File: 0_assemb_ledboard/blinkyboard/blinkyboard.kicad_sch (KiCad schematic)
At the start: 61 parts, among them J1 Conn_01x05, U1 LM2902, U2 LM2902, U3 LM2902, U4 LM2902

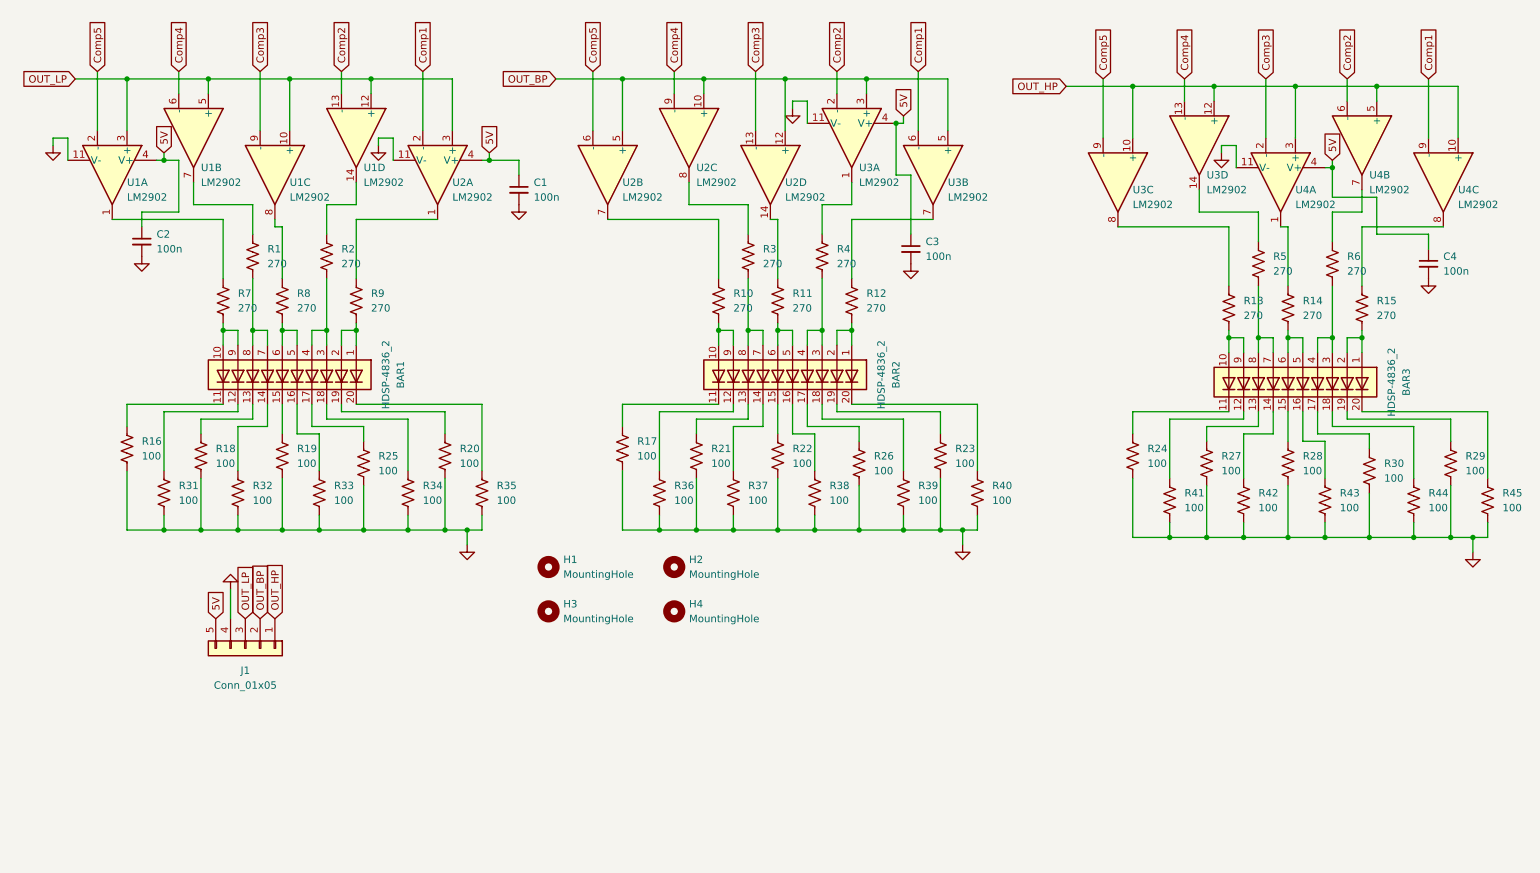
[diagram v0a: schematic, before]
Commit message: Fixed LED Board and added GND to SPI on Main Board
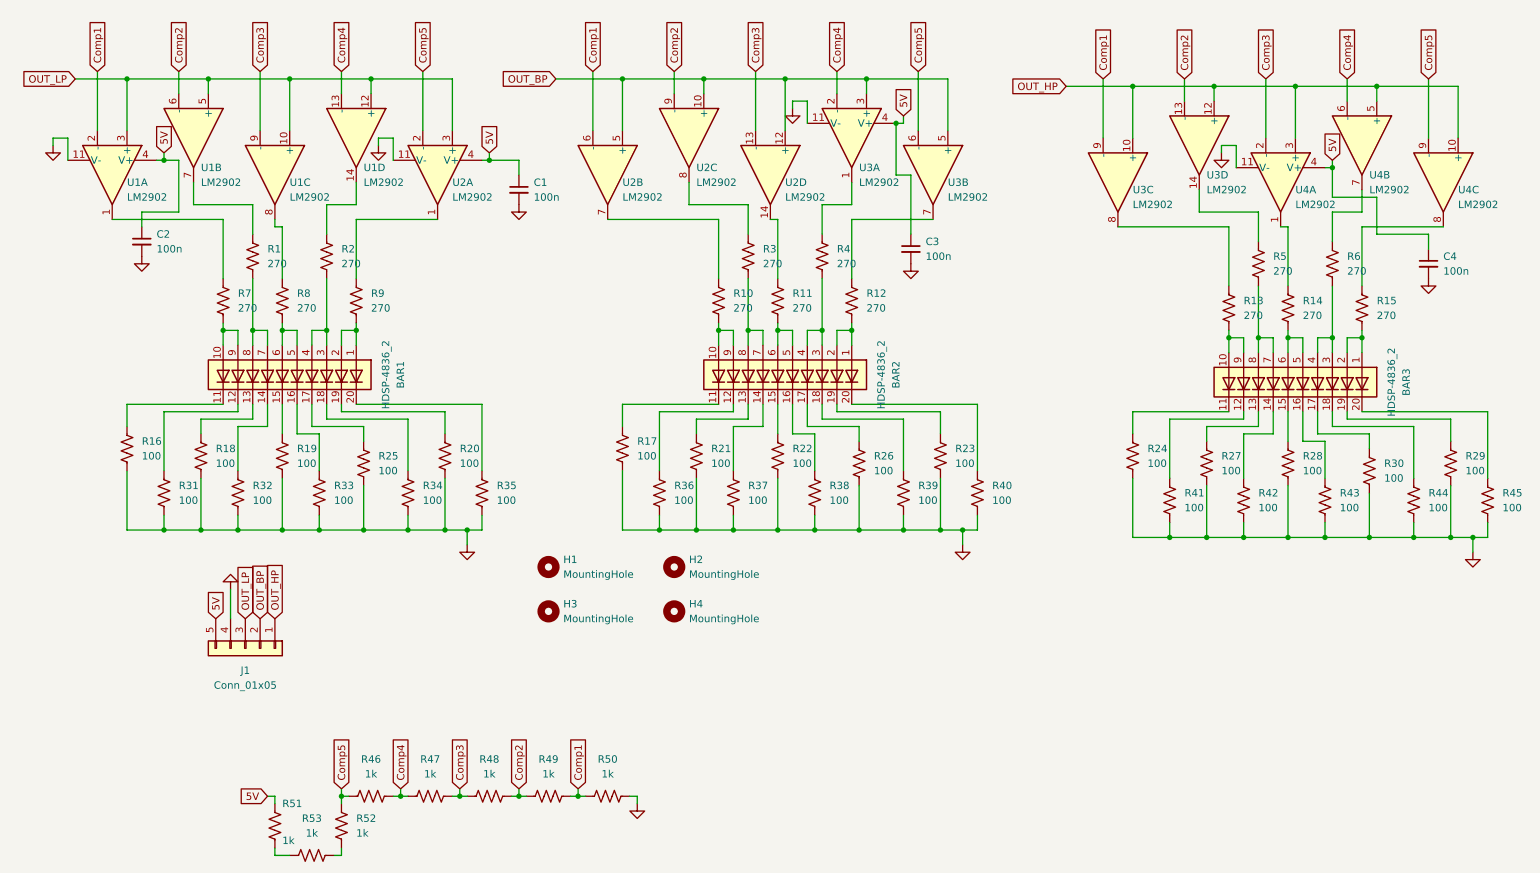
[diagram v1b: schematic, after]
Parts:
- added R46, R47, R48, R49, R50, R51, R52, R53: 1k, Resistor_SMD:R_0805_2012Metric_Pad1.20x1.40mm_HandSolder, symbol Device:R_US
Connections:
- net 5V: now also R51.2
- net Comp1: now also U1.2 (-), U2.6 (-), U3.9 (-), R49.1, R50.2; no longer U2.2 (-), U3.6 (-), U4.9 (-)
- net Comp2: now also U1.6 (-), U2.9 (-), U3.13 (-), R48.1, R49.2; no longer U1.13 (-), U3.2 (-), U4.6 (-)
- net Comp3: now also R47.1, R48.2
- net Comp4: now also U1.13 (-), U3.2 (-), U4.6 (-), R46.1, R47.2; no longer U1.6 (-), U2.9 (-), U3.13 (-)
- net Comp5: now also U2.2 (-), U3.6 (-), U4.9 (-), R46.2, R52.2; no longer U1.2 (-), U2.6 (-), U3.9 (-)
- net GND: now also R50.1
- new net: R51.1, R53.2
- new net: R52.1, R53.1
